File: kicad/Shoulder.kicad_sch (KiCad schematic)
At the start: 9 parts, among them U301 NSP4201MR6

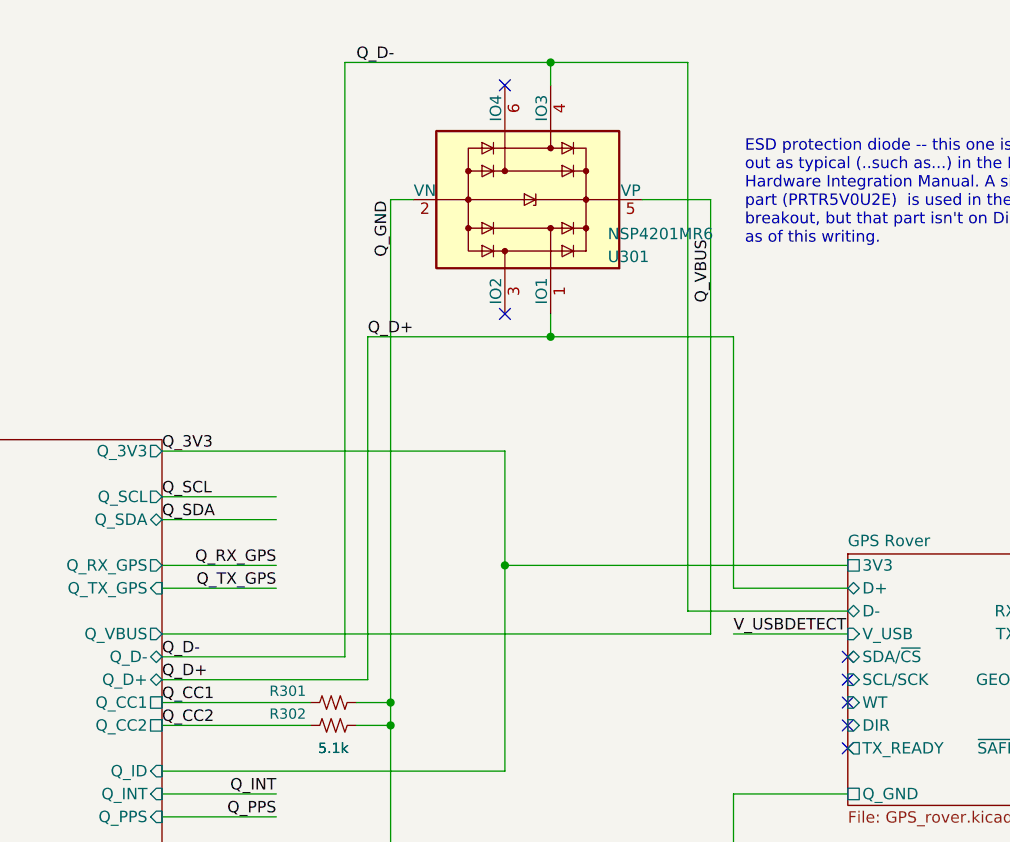
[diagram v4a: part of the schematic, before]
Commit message: Updated which lines are used in 4-line protection diode
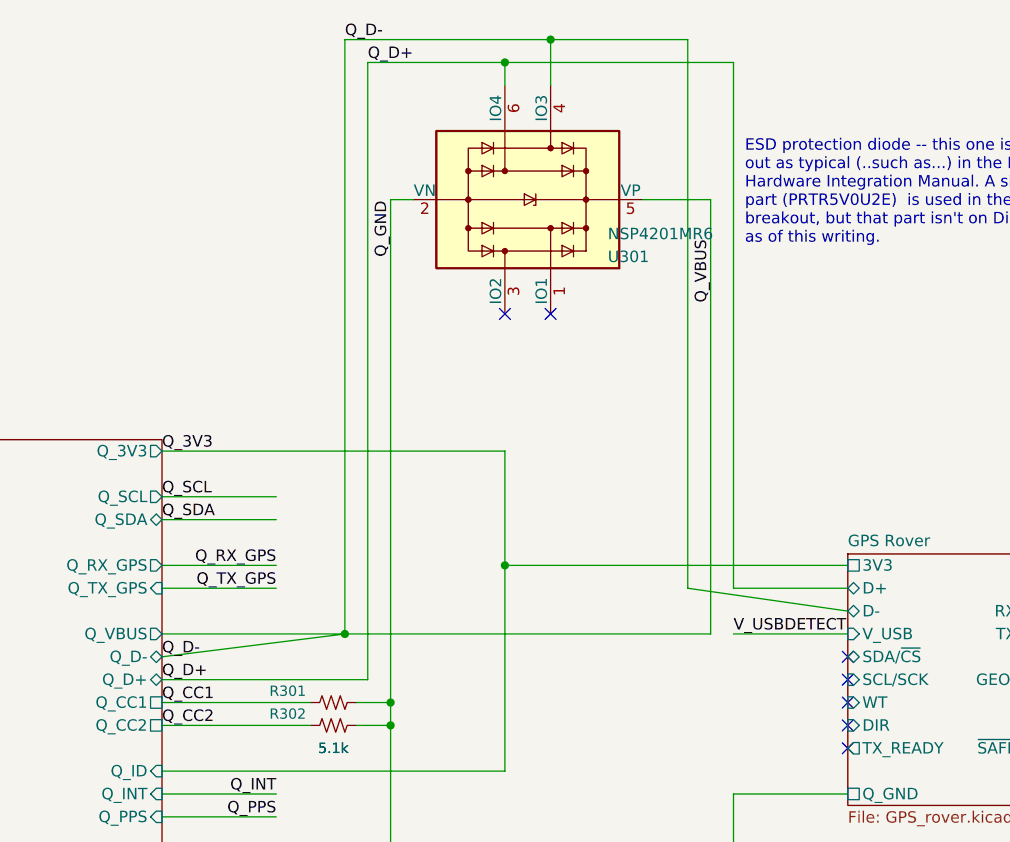
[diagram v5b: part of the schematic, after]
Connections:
- net Q_VBUS is gone; now on net Q_D-: U301.5 (VP)
- net Q_D+: now also U301.6 (IO4); no longer U301.1 (IO1)
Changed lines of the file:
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@@
   (junction (at 165.1 114.3) (diameter 0) (color 0 0 0 0)
   )
+  (junction (at 177.8 20.32) (diameter 0) (color 0 0 0 0)
+  )
   (junction (at 177.8 76.2) (diameter 0) (color 0 0 0 0)
   )
-  (junction (at 182.88 20.32) (diameter 0) (color 0 0 0 0)
+  (junction (at 182.88 17.78) (diameter 0) (color 0 0 0 0)
   )
   (junction (at 165.1 93.98) (diameter 0) (color 0 0 0 0)
   )
-  (junction (at 182.88 50.8) (diameter 0) (color 0 0 0 0)
+  (junction (at 160.02 83.82) (diameter 0) (color 0 0 0 0)
   )
   (junction (at 35.56 165.1) (diameter 0) (color 0 0 0 0)
@@
   )
   (no_connect (at 215.9 96.52))
-  (no_connect (at 177.8 22.86))
+  (no_connect (at 182.88 48.26))
   (no_connect (at 139.7 109.22))
-  (no_connect (at 177.8 48.26))
   (no_connect (at 215.9 93.98))
   (no_connect (at 215.9 91.44))
@@
   (no_connect (at 241.3 76.2))
   (no_connect (at 241.3 78.74))
+  (no_connect (at 177.8 48.26))
   (wire (pts (xy 241.3 83.82) (xy 254 83.82))
     (stroke (width 0) (type default) (color 0 0 0 0))
@@
     (stroke (width 0) (type default) (color 0 0 0 0))
   )
-  (wire (pts (xy 215.9 81.28) (xy 198.12 81.28))
+  (wire (pts (xy 215.9 81.28) (xy 198.12 78.74))
     (stroke (width 0) (type default) (color 0 0 0 0))
   )
@@
     (stroke (width 0) (type default) (color 0 0 0 0))
   )
-  (wire (pts (xy 139.7 83.82) (xy 200.66 83.82))
+  (wire (pts (xy 139.7 83.82) (xy 160.02 83.82))
     (stroke (width 0) (type default) (color 0 0 0 0))
   )
@@
     (stroke (width 0) (type default) (color 0 0 0 0))
   )
+  (wire (pts (xy 160.02 83.82) (xy 200.66 83.82))
+    (stroke (width 0) (type default) (color 0 0 0 0))
+  )
   (wire (pts (xy 101.6 99.06) (xy 110.49 99.06))
     (stroke (width 0) (type default) (color 0 0 0 0))
@@
     (stroke (width 0) (type default) (color 0 0 0 0))
   )
-  (wire (pts (xy 182.88 50.8) (xy 182.88 48.26))
-    (stroke (width 0) (type default) (color 0 0 0 0))
-  )
   (wire (pts (xy 101.6 101.6) (xy 110.49 101.6))
     (stroke (width 0) (type default) (color 0 0 0 0))
@@
     (stroke (width 0) (type default) (color 0 0 0 0))
   )
-  (wire (pts (xy 198.12 81.28) (xy 198.12 20.32))
-    (stroke (width 0) (type default) (color 0 0 0 0))
-  )
-  (wire (pts (xy 160.02 20.32) (xy 182.88 20.32))
+  (wire (pts (xy 198.12 78.74) (xy 198.12 17.78))
+    (stroke (width 0) (type default) (color 0 0 0 0))
+  )
+  (wire (pts (xy 160.02 17.78) (xy 182.88 17.78))
     (stroke (width 0) (type default) (color 0 0 0 0))
   )
@@
     (stroke (width 0) (type default) (color 0 0 0 0))
   )
-  (wire (pts (xy 182.88 20.32) (xy 198.12 20.32))
+  (wire (pts (xy 182.88 17.78) (xy 198.12 17.78))
     (stroke (width 0) (type default) (color 0 0 0 0))
   )
@@
     (stroke (width 0) (type default) (color 0 0 0 0))
   )
-  (wire (pts (xy 162.56 88.9) (xy 162.56 50.8))
+  (wire (pts (xy 162.56 88.9) (xy 162.56 20.32))
     (stroke (width 0) (type default) (color 0 0 0 0))
   )
@@
     (stroke (width 0) (type default) (color 0 0 0 0))
   )
-  (wire (pts (xy 160.02 86.36) (xy 160.02 20.32))
-    (stroke (width 0) (type default) (color 0 0 0 0))
-  )
-  (wire (pts (xy 203.2 50.8) (xy 203.2 78.74))
+  (wire (pts (xy 160.02 83.82) (xy 160.02 17.78))
+    (stroke (width 0) (type default) (color 0 0 0 0))
+  )
+  (wire (pts (xy 203.2 20.32) (xy 203.2 78.74))
     (stroke (width 0) (type default) (color 0 0 0 0))
   )
@@
     (stroke (width 0) (type default) (color 0 0 0 0))
   )
-  (wire (pts (xy 139.7 86.36) (xy 160.02 86.36))
-    (stroke (width 0) (type default) (color 0 0 0 0))
-  )
-  (wire (pts (xy 182.88 50.8) (xy 203.2 50.8))
+  (wire (pts (xy 139.7 86.36) (xy 160.02 83.82))
+    (stroke (width 0) (type default) (color 0 0 0 0))
+  )
+  (wire (pts (xy 177.8 20.32) (xy 203.2 20.32))
+    (stroke (width 0) (type default) (color 0 0 0 0))
+  )
+  (wire (pts (xy 162.56 20.32) (xy 177.8 20.32))
+    (stroke (width 0) (type default) (color 0 0 0 0))
+  )
+  (wire (pts (xy 177.8 20.32) (xy 177.8 22.86))
     (stroke (width 0) (type default) (color 0 0 0 0))
   )
@@
     (stroke (width 0) (type default) (color 0 0 0 0))
   )
-  (wire (pts (xy 182.88 20.32) (xy 182.88 22.86))
+  (wire (pts (xy 182.88 17.78) (xy 182.88 22.86))
     (stroke (width 0) (type default) (color 0 0 0 0))
   )
@@
   )
   (wire (pts (xy 101.6 78.74) (xy 110.49 78.74))
-    (stroke (width 0) (type default) (color 0 0 0 0))
-  )
-  (wire (pts (xy 162.56 50.8) (xy 182.88 50.8))
     (stroke (width 0) (type default) (color 0 0 0 0))
   )
@@
     (effects (font (size 1.27 1.27)) (justify left bottom))
   )
-  (label "Q_D+" (at 162.56 50.8 0)
+  (label "Q_D+" (at 162.56 20.32 0)
     (effects (font (size 1.27 1.27)) (justify left bottom))
   )
@@
     (effects (font (size 1.27 1.27)) (justify left bottom))
   )
-  (label "Q_D-" (at 161.29 20.32 0)
-    (effects (font (size 1.27 1.27)) (justify left bottom))
-  )
+  (label "Q_D-" (at 160.02 17.78 0)
+    (effects (font (size 1.27 1.27)) (justify left bottom))
+  )
